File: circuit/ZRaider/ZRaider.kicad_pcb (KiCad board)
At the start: 2 copper layers, 110 x 56 mm, 20 parts, among them J1 DE9_Socket, SW1 UP, SW2 DOWN, SW3 LEFT, SW4 RIGHT, SW5 Trigger, SW6 Calibrate

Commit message: adding last remaining connections
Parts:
- C1: moved to B.Cu
- turned C1 to -90 degrees
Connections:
- A1 pad 4: unconnected-(A1-GND-Pad4) -> Net-(A1-GND-Pad29)
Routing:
- net Net-(A1-GND-Pad29): track 242.5 -> 273.3 mm
- net Net-(A1-A1): track 33.4 -> 28.4 mm

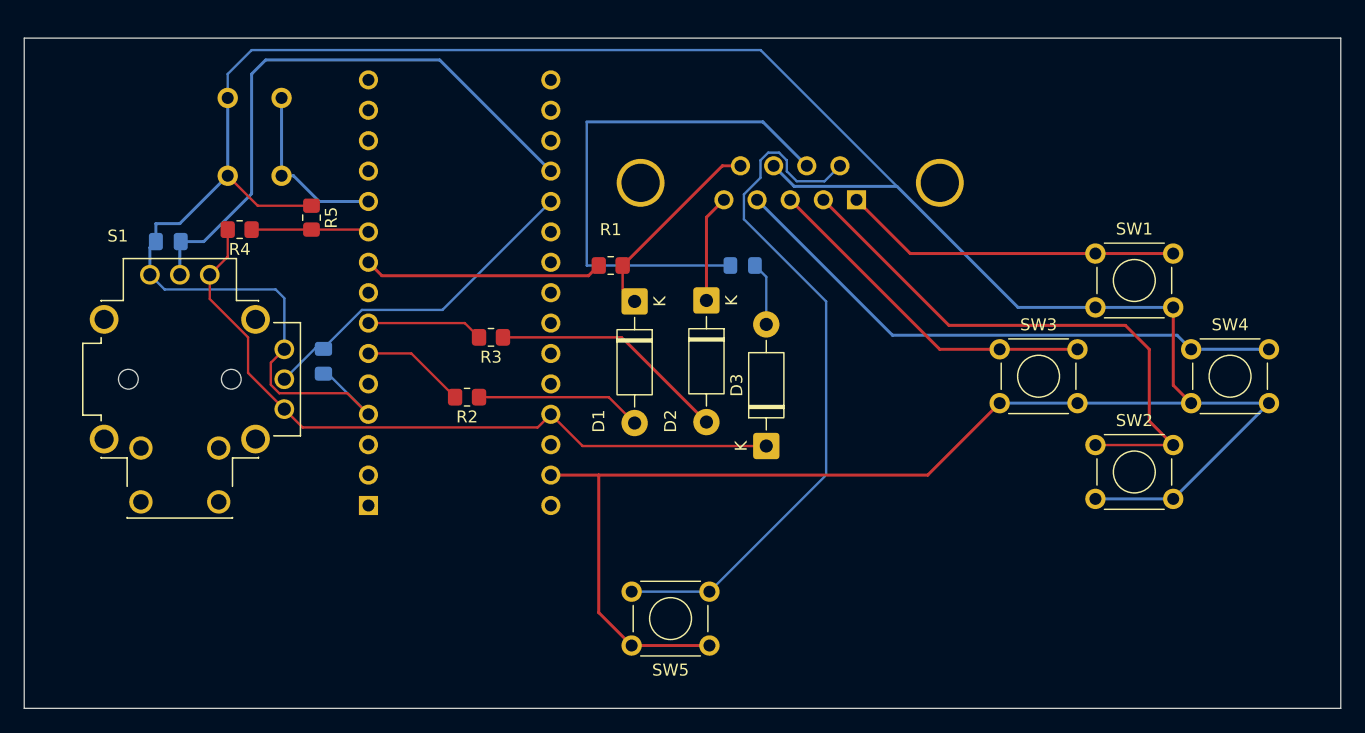
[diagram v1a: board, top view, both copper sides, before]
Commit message: updating layout to accomodate J1 size (actual) vs library
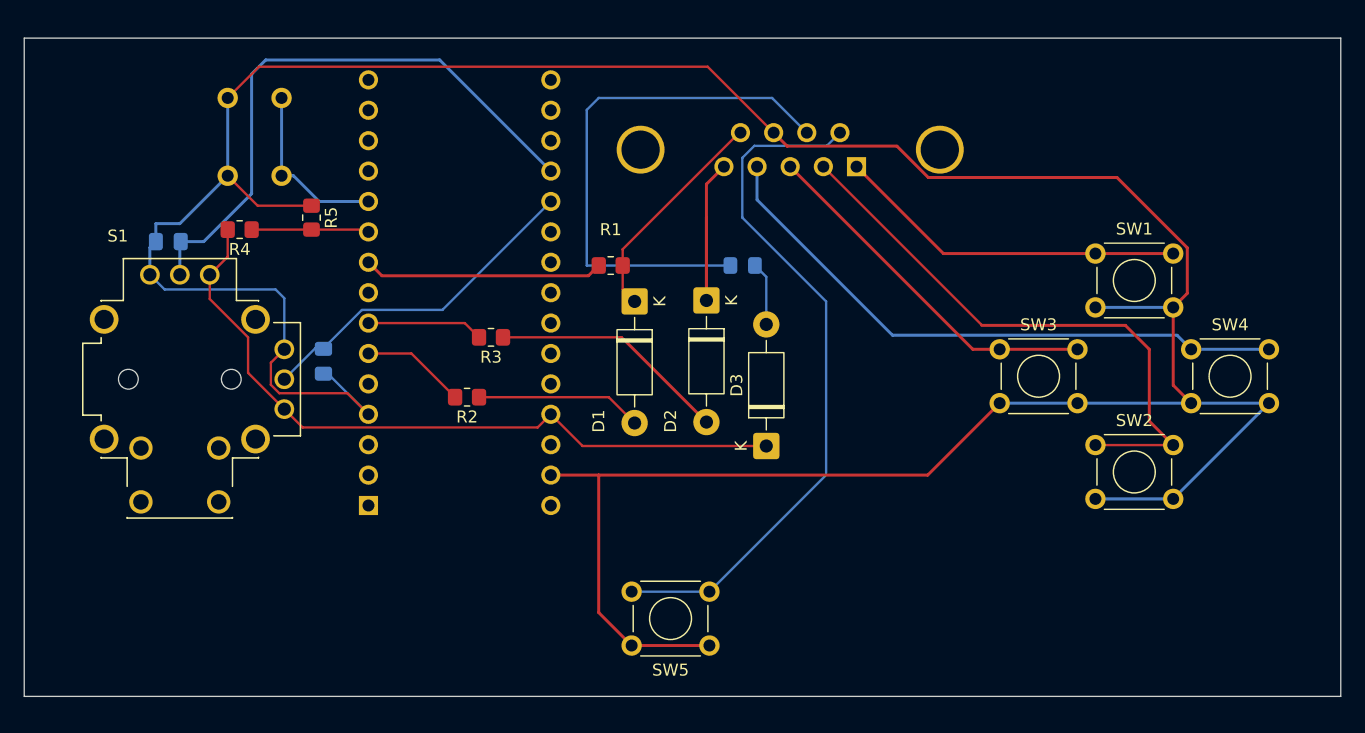
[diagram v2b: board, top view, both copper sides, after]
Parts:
- moved J1 2.77 mm to (129.5, 59.7)
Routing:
- net Net-(D2-K): track 9.01 -> 18.7 mm
- net Net-(J1-Pad4): track 47.9 -> 50.7 mm
- net Net-(A1-GND-Pad29): track 273.3 -> 271.1 mm
- net Net-(J1-Pad3): track 29.2 -> 31.2 mm
- net Net-(D1-K): track 16.7 -> 18.7 mm
- net Net-(J1-Pad2): track 47.7 -> 48.9 mm
- net Net-(J1-Pad1): track 28.3 -> 29.5 mm
- net Net-(F1-Pad1): track 43.9 -> 45.0 mm
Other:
- board size 110 x 56 mm -> 110 x 55 mm

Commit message: adding mounting holes
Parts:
- added REF**: MountingHole_3.2mm_M3, MountingHole:MountingHole_3.2mm_M3, F.Cu at (166.0, 53.0)
- added REF**: MountingHole_3.2mm_M3, MountingHole:MountingHole_3.2mm_M3, F.Cu at (64.0, 53.0)
- added REF**: MountingHole_3.2mm_M3, MountingHole:MountingHole_3.2mm_M3, F.Cu at (166.0, 100.0)
- added REF**: MountingHole_3.2mm_M3, MountingHole:MountingHole_3.2mm_M3, F.Cu at (64.0, 100.0)
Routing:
- net Net-(D2-K): track 18.7 -> 11.8 mm

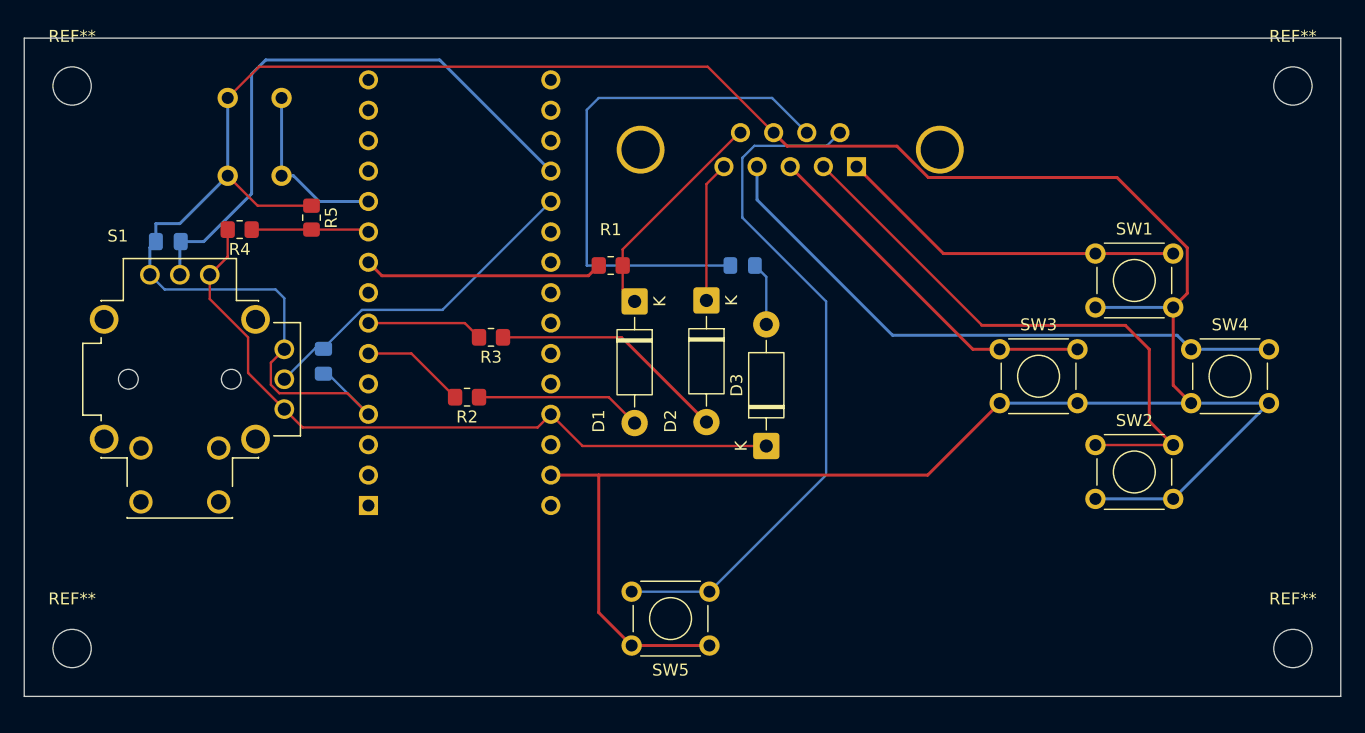
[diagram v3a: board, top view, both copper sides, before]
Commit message: tweaking board size based on DB9's I've got onhand
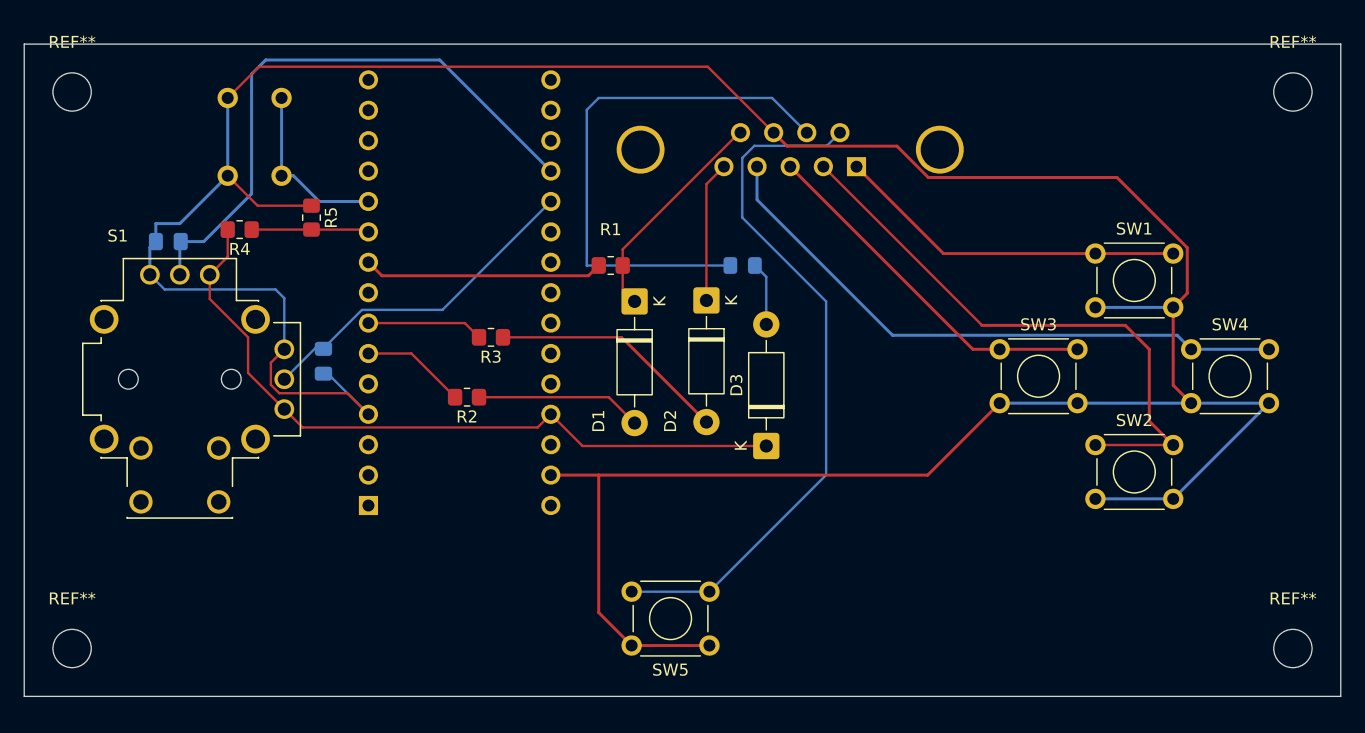
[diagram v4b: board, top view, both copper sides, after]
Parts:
- moved REF** 0.50 mm to (166.0, 53.5)
- moved REF** 0.50 mm to (64.0, 53.5)
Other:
- board size 110 x 55 mm -> 110 x 54.5 mm
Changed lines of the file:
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@@
 			(outputformat 1)
 			(mirror no)
-			(drillshape 1)
+			(drillshape 0)
 			(scaleselection 1)
-			(outputdirectory "")
+			(outputdirectory "./Gerbers")
 		)
 	)
 	(footprint "MountingHole:MountingHole_3.2mm_M3"
 		(layer "F.Cu")
-		(at 166 53)
+		(at 166 53.5)
 		(descr "Mounting Hole 3.2mm, M3, no annular, generated by kicad-footprint-generator mountinghole.py")
 		(tags "mountinghole M3")
@@
 	(footprint "MountingHole:MountingHole_3.2mm_M3"
 		(layer "F.Cu")
-		(at 64 53)
+		(at 64 53.5)
 		(descr "Mounting Hole 3.2mm, M3, no annular, generated by kicad-footprint-generator mountinghole.py")
 		(tags "mountinghole M3")
@@
 	)
 	(gr_rect
-		(start 60 49)
+		(start 60 49.5)
 		(end 170 104)
 		(stroke

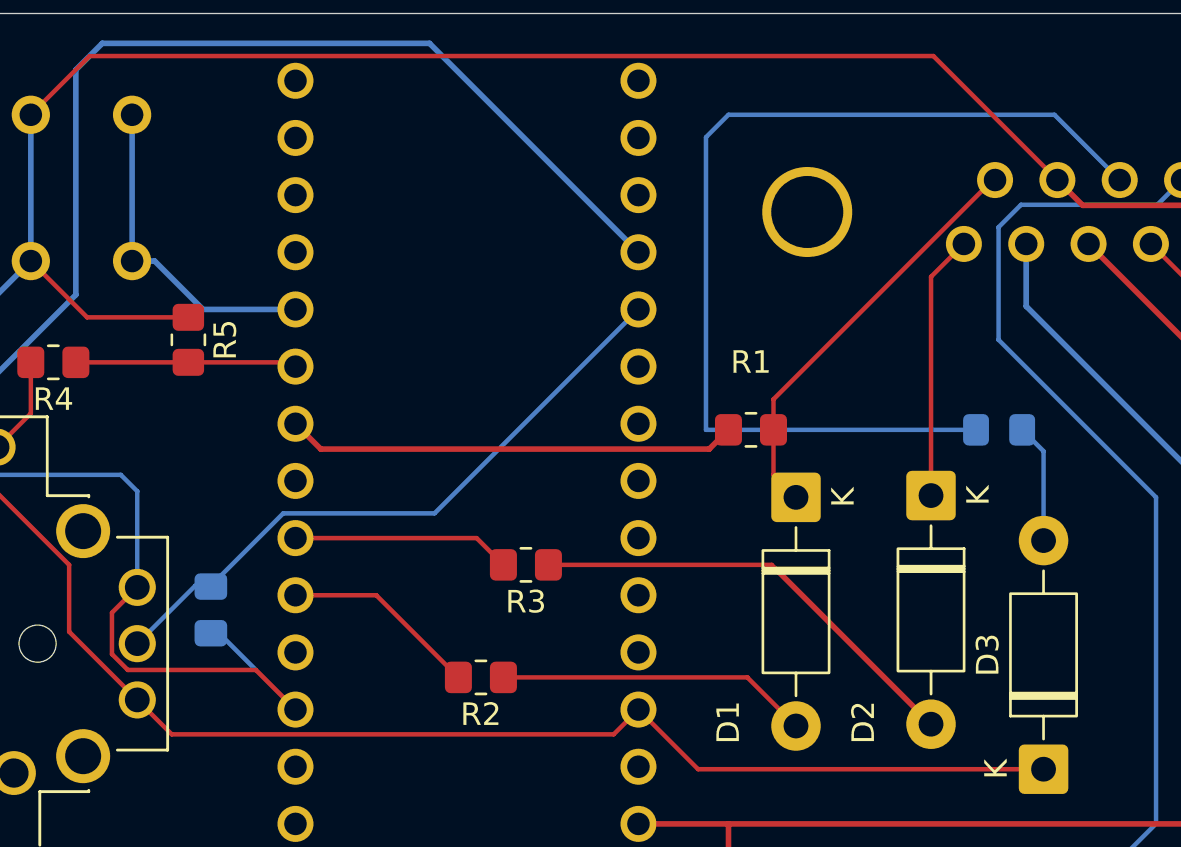
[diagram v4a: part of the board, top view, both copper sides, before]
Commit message: updating fuse footprint
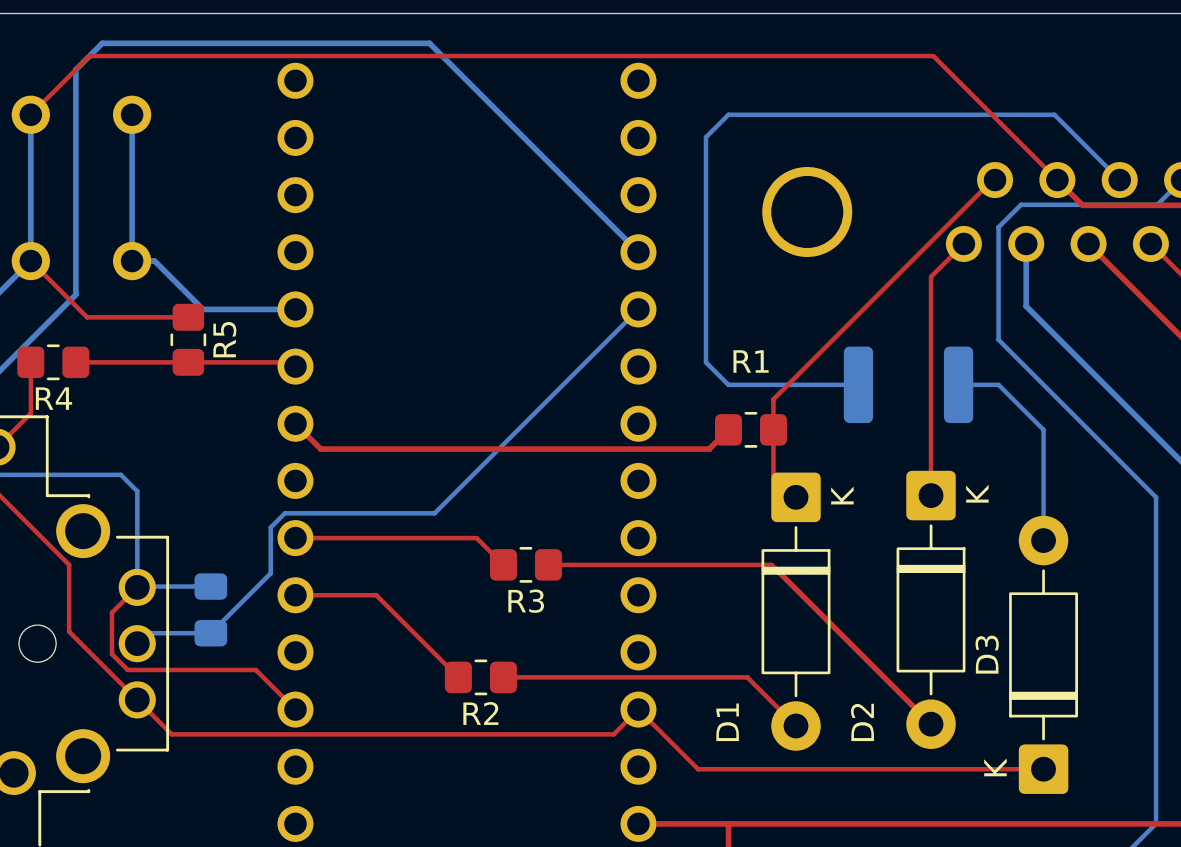
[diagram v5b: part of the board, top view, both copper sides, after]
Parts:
- F1: footprint Fuse:Fuse_0805_2012Metric_Pad1.15x1.40mm_HandSolder -> Fuse:Fuse_1812_4532Metric_Pad1.30x3.40mm_HandSolder
- moved F1 4.49 mm to (116.0, 66.0)
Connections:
- C1 pad 1: Net-(A1-A1) -> Net-(A1-GND-Pad29)
- C1 pad 2: Net-(A1-GND-Pad29) -> Net-(A1-A1)
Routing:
- net Net-(F1-Pad1): track 45.0 -> 37.2 mm
- net Net-(D3-A): track 5.31 -> 9.52 mm
- net Net-(A1-A1): track 28.4 -> 29.9 mm
- net Net-(A1-GND-Pad29): track 271.1 -> 269.9 mm
